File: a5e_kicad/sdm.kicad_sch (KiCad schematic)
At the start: 24 parts, among them U2 W25X20CLZP, U7 A5EB013B-B23B

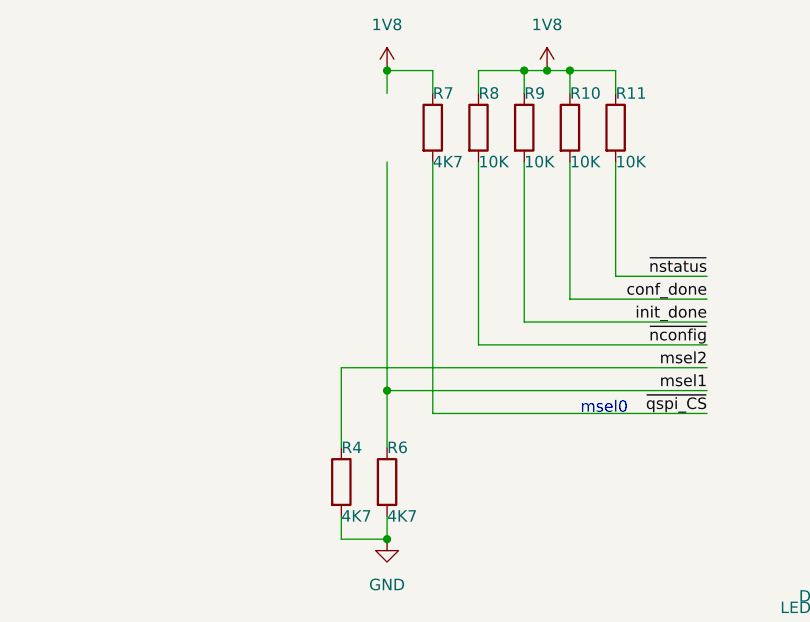
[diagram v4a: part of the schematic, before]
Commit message: route more rgmii io
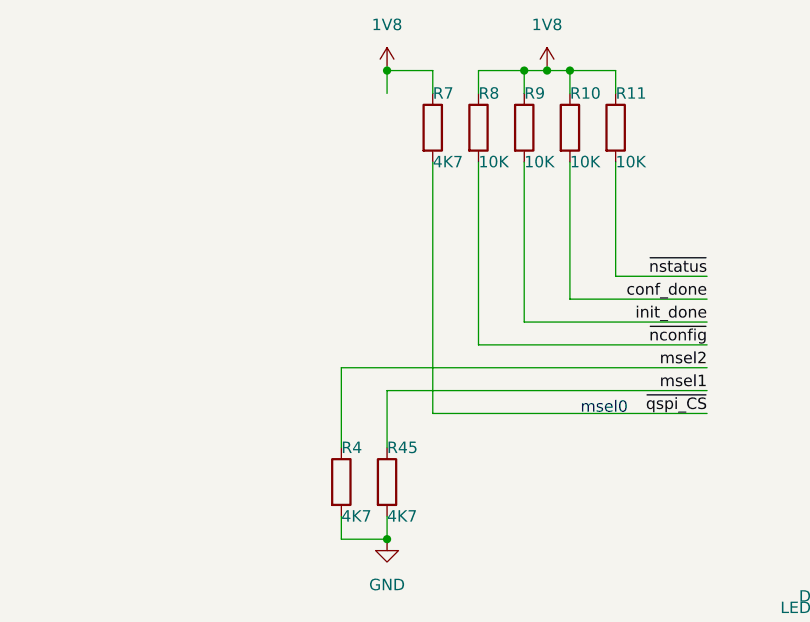
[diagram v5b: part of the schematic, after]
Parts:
- removed R6: 4K7, Resistor_SMD:R_0402_1005Metric, symbol Device:R
- added R45: 4K7, Resistor_SMD:R_0402_1005Metric, symbol Device:R
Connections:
- net GND: now also R45.2
- net msel1: now also R45.1

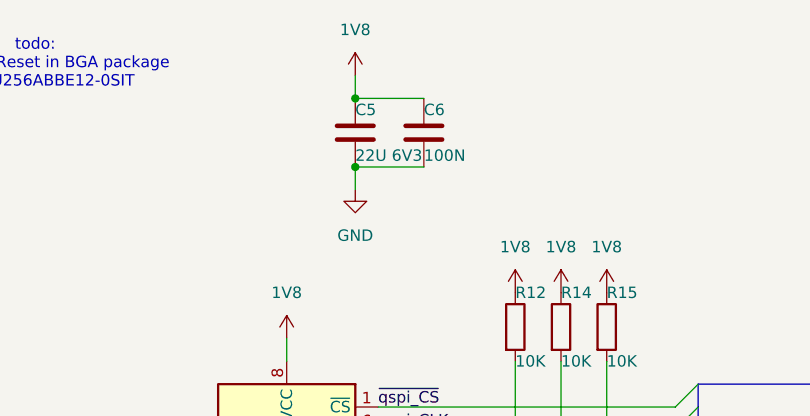
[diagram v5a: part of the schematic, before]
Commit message: remove extra components and make 1v8 plane
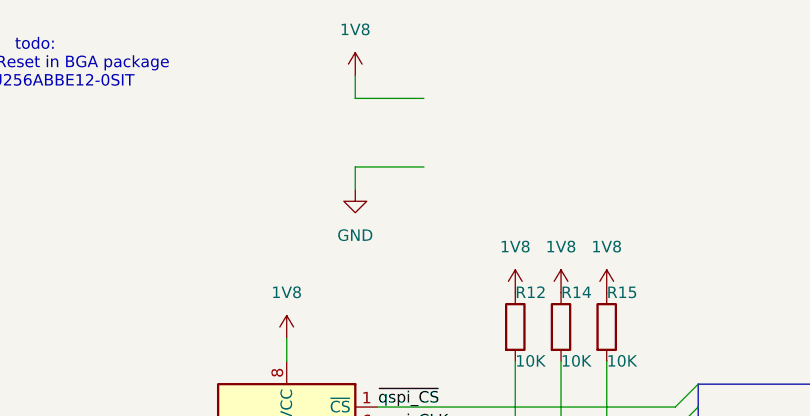
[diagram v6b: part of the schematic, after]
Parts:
- removed C5: 22U 6V3, Capacitor_SMD:C_0402_1005Metric, symbol Device:C
- removed C6: 100N, Capacitor_SMD:C_0402_1005Metric, symbol Device:C
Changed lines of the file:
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@@
 	)
 	(junction
-		(at 66.04 29.21)
-		(diameter 0)
-		(color 0 0 0 0)
-	)
-	(junction
 		(at 58.42 76.2)
 		(diameter 0)
@@
 	)
 	(junction
-		(at 66.04 21.59)
-		(diameter 0)
-		(color 0 0 0 0)
-	)
-	(junction
 		(at 220.98 20.32)
 		(diameter 0)
@@
 	)
 	(symbol
-		(lib_id "Device:C")
-		(at 73.66 25.4 0)
-		(unit 1)
-		(body_style 1)
-		(exclude_from_sim no)
-		(in_bom yes)
-		(on_board yes)
-		(in_pos_files yes)
-		(dnp no)
-		(property "Reference" "C6"
-			(at 73.66 22.86 0)
-			(show_name no)
-			(do_not_autoplace no)
-			(effects
-				(font
-					(size 1.27 1.27)
-				)
-				(justify left)
-			)
-		)
-		(property "Value" "100N"
-			(at 73.66 27.94 0)
-			(show_name no)
-			(do_not_autoplace no)
-			(effects
-				(font
-					(size 1.27 1.27)
-				)
-				(justify left)
-			)
-		)
-		(property "Footprint" "Capacitor_SMD:C_0402_1005Metric"
-			(at 74.6252 29.21 0)
-			(hide yes)
-			(show_name no)
-			(do_not_autoplace no)
-			(effects
-				(font
-					(size 1.27 1.27)
-				)
-			)
-		)
-		(property "Datasheet" ""
-			(at 73.66 25.4 0)
-			(hide yes)
-			(show_name no)
-			(do_not_autoplace no)
-			(effects
-				(font
-					(size 1.27 1.27)
-				)
-			)
-		)
-		(property "Description" "Unpolarized capacitor"
-			(at 73.66 25.4 0)
-			(hide yes)
-			(show_name no)
-			(do_not_autoplace no)
-			(effects
-				(font
-					(size 1.27 1.27)
-				)
-			)
-		)
-		(pin "1"
-		)
-		(pin "2"
-		)
-		(instances
-			(project ""
-				(path "/267d02d2-570f-41a1-8015-b378cedbc665/8aaf6c2b-ae6e-4499-806d-67948f95803c"
-					(reference "C202")
-					(unit 1)
-				)
-			)
-			(project "agilex_3_soc"
-				(path "/a5b98d95-6877-4284-904f-d04e32723ae0/8aaf6c2b-ae6e-4499-806d-67948f95803c"
-					(reference "C6")
-					(unit 1)
-				)
-			)
-		)
-	)
-	(symbol
 		(lib_id "Device:R")
 		(at 215.9 26.67 0)
@@
 					(unit 1)
 				)
-			)
-		)
-	)
-	(symbol
-		(lib_id "Device:C")
-		(at 66.04 25.4 0)
-		(unit 1)
-		(body_style 1)
-		(exclude_from_sim no)
-		(in_bom yes)
-		(on_board yes)
-		(in_pos_files yes)
-		(dnp no)
-		(property "Reference" "C5"
-			(at 66.04 22.86 0)
-			(show_name no)
-			(do_not_autoplace no)
-			(effects
-				(font
-					(size 1.27 1.27)
-				)
-				(justify left)
-			)
-		)
-		(property "Value" "22U 6V3"
-			(at 66.04 27.94 0)
-			(show_name no)
-			(do_not_autoplace no)
-			(effects
-				(font
-					(size 1.27 1.27)
-				)
-				(justify left)
-			)
-		)
-		(property "Footprint" "Capacitor_SMD:C_0402_1005Metric"
-			(at 67.0052 29.21 0)
-			(hide yes)
-			(show_name no)
-			(do_not_autoplace no)
-			(effects
-				(font
-					(size 1.27 1.27)
-				)
-			)
-		)
-		(property "Datasheet" ""
-			(at 66.04 25.4 0)
-			(hide yes)
-			(show_name no)
-			(do_not_autoplace no)
-			(effects
-				(font
-					(size 1.27 1.27)
-				)
-			)
-		)
-		(property "Description" "Unpolarized capacitor"
-			(at 66.04 25.4 0)
-			(hide yes)
-			(show_name no)
-			(do_not_autoplace no)
-			(effects
-				(font
-					(size 1.27 1.27)
-				)
-			)
-		)
-		(pin "1"
-		)
-		(pin "2"
-		)
-		(instances
-			(project "DBM_A5E013"
-				(path "/267d02d2-570f-41a1-8015-b378cedbc665/8aaf6c2b-ae6e-4499-806d-67948f95803c"
-					(reference "C201")
-					(unit 1)
-				)
-			)
-			(project "agilex_3_soc"
-				(path "/a5b98d95-6877-4284-904f-d04e32723ae0/8aaf6c2b-ae6e-4499-806d-67948f95803c"
-					(reference "C5")
-					(unit 1)
-				)
